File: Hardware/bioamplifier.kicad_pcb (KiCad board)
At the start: 4 copper layers, 70 x 40 mm, 92 parts, among them IC1 MCP1754ST-3302E_DB, J1 Conn_01x07_Socket, J2 Conn_01x26_Pin, J3 Conn_01x07_Socket, U1 ADS1299IPAG, U10 TPD4E1B06DCKR, U11 LM2665M6, U2 TPD4E1B06DCKR, U3 TPD4E1B06DCKR, U4 TPD4E1B06DCKR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

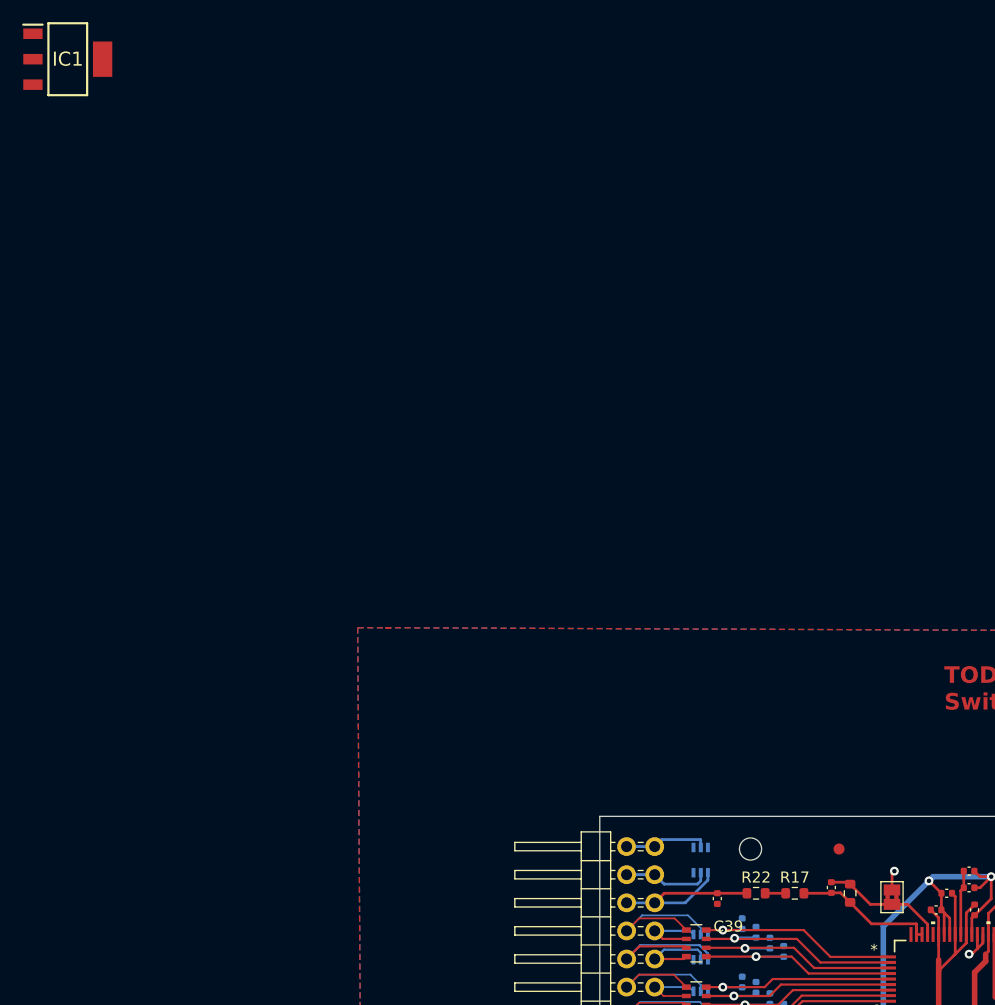
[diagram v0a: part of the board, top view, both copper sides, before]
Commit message: Remove redundant components
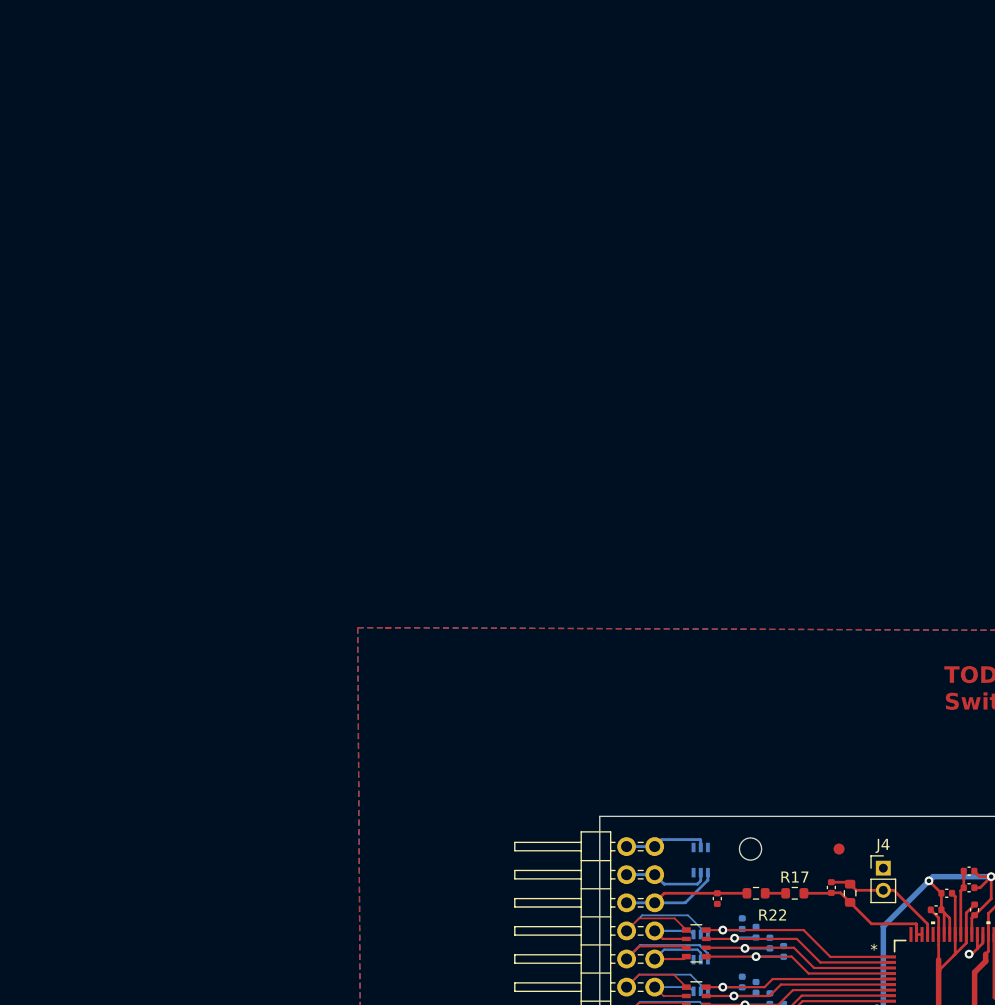
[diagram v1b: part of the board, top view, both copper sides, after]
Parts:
- removed IC1: MCP1754ST-3302E_DB, mcp1754:SOT230P700X180-4N
- removed JP2: Jumper_2_Bridged, Jumper:SolderJumper-2_P1.3mm_Bridged2Bar_Pad1.0x1.5mm
- added J4: Jumper, Connector_PinHeader_2.00mm:PinHeader_1x02_P2.00mm_Vertical, F.Cu at (78.0, 76.7)
- C25, C40: value 0.1u -> 0.1uF
- C45, C46: value 10 u -> 10 uF
- R1: value 1K -> 1 KΩ
- R10, R11, R12, R13, R14, R3, R4, R5, R6, R7, R8, R9: value 50 -> 50 Ω
- R17: value 1M -> 1 MΩ
- R18, R2, R20, R22, RN1, RN2, RN3, RN4: value 4.99 K -> 4.99 KΩ
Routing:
- net GNDA: track 33.5 -> 31.7 mm, vias 8 -> 7

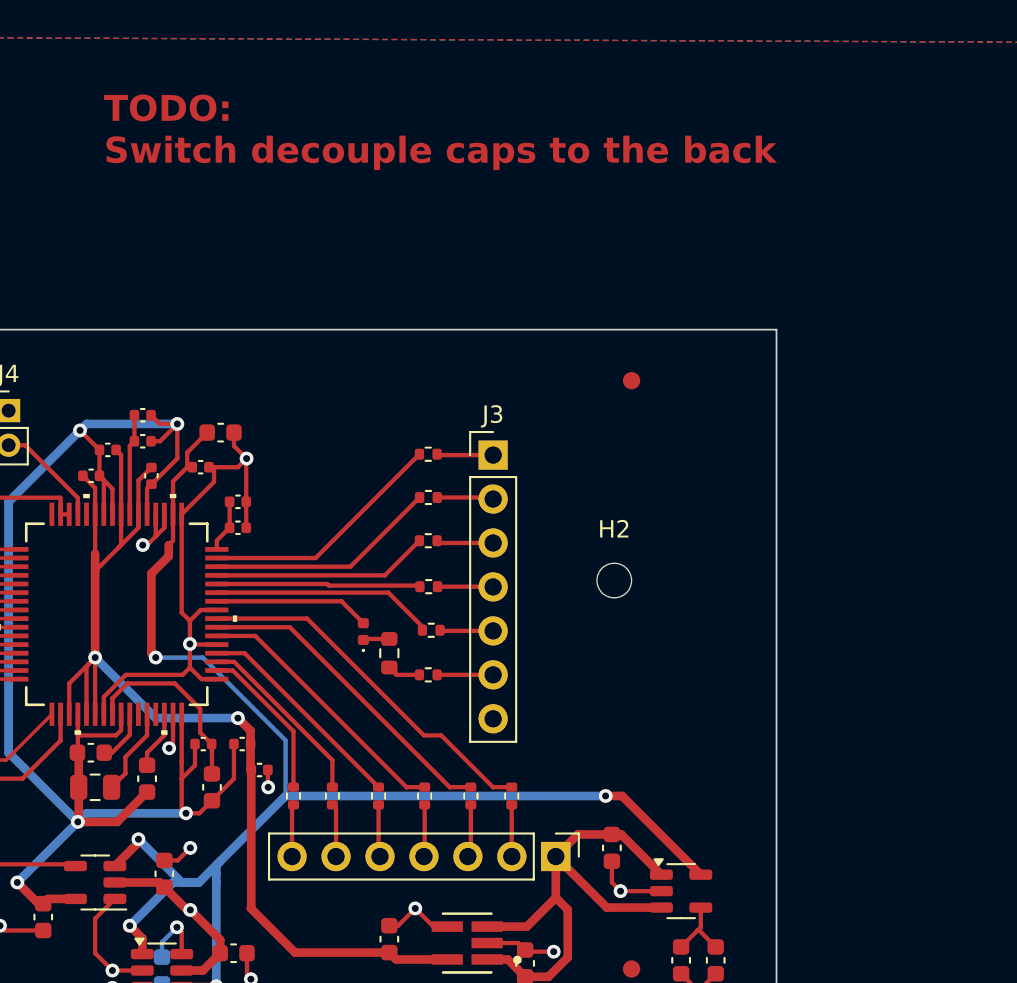
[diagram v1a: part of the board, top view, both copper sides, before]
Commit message: Add Daisychain jumper
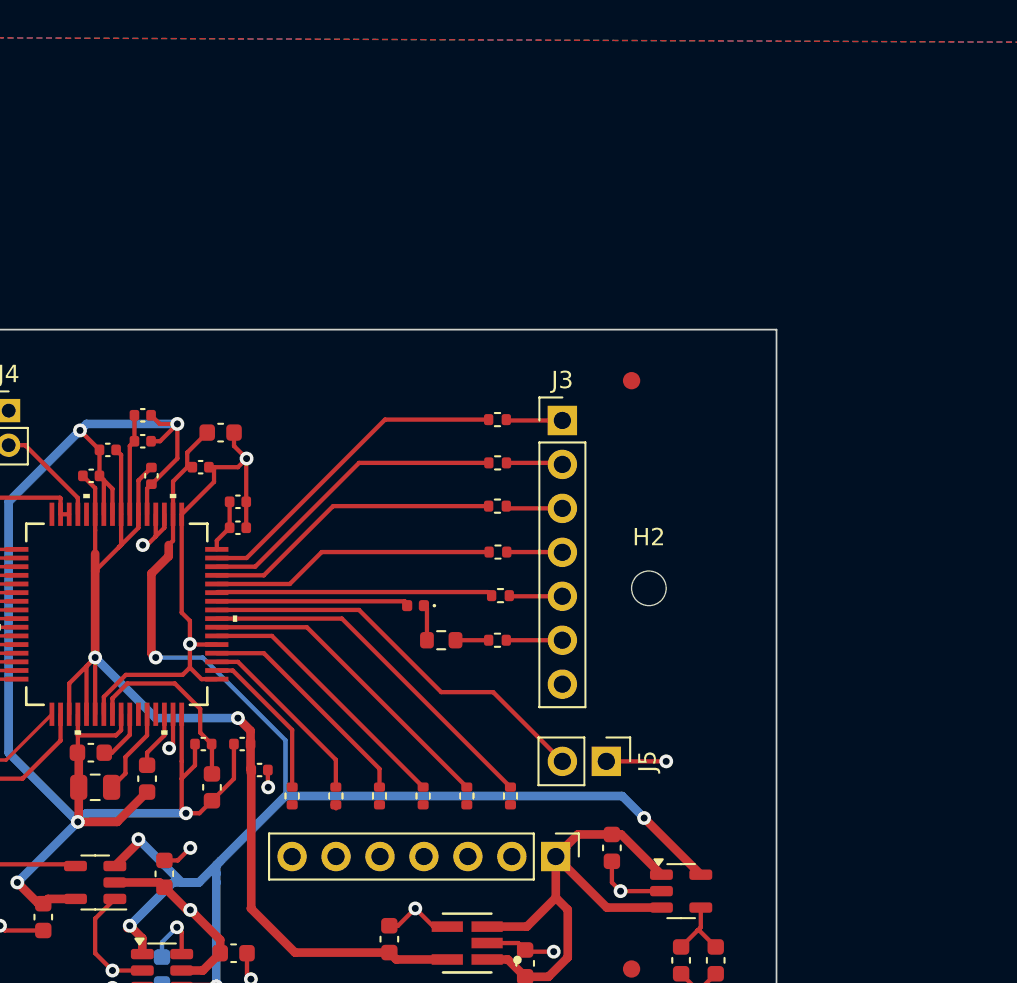
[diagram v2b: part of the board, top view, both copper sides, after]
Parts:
- added J5: Jumper, Connector_PinHeader_2.54mm:PinHeader_1x02_P2.54mm_Vertical, F.Cu at (112.5, 97.0)
- D1: value BLUE LED -> LB QH9G-N1OO-35-1
- RN1, RN2, RN3, RN4: value 4.99 KΩ -> EXB-V8V512JV
- moved J3 4.47 mm to (110.0, 77.3)
- moved R3 4.47 mm to (106.2, 77.2)
- moved R4 4.47 mm to (106.3, 79.8)
- moved R5 4.47 mm to (106.2, 82.2)
- moved R6 4.47 mm to (106.3, 84.9)
- moved R7 4.47 mm to (106.4, 87.4)
- moved R8 4.47 mm to (106.2, 90.0)
- moved D1 3.37 mm to (101.5, 88.0), turned to 180 degrees
- moved R1 3.09 mm to (103.0, 90.0), turned to 0 degrees
- moved H2 2.05 mm to (115.0, 87.0)
- moved R10 0.23 mm to (104.5, 99.0)
- moved R13 0.20 mm to (96.9, 99.0)
- moved R11 0.09 mm to (102.0, 99.0)
- moved R9 0.07 mm to (107.0, 99.0)
- moved R14 0.07 mm to (94.4, 99.0)
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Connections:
- U1 pad 41: GNDD -> /DAISY-IN
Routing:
- net /DAISY-IN: track 0.00 -> 23.6 mm
- net /GPIO4: track 13.4 -> 18.2 mm
- net /GPIO3: track 12.5 -> 17.4 mm
- net /DRDY: track 14.2 -> 19.0 mm
- net /GPIO2: track 11.8 -> 16.5 mm
- net /DOUT: track 12.9 -> 16.0 mm
- net Net-(J1-Pin_2): track 2.99 -> 0.01 mm
- net Net-(J1-Pin_4): track 3.01 -> 0.06 mm
- net Net-(J1-Pin_7): track 3.02 -> 0.11 mm
- net Net-(J1-Pin_5): track 3.02 -> 0.12 mm
- net Net-(J1-Pin_3): track 3.06 -> 0.24 mm
- net Net-(J1-Pin_6): track 3.08 -> 0.30 mm
- net Net-(D1-A): track 9.00 -> 11.0 mm
- net GNDD: track 44.9 -> 46.6 mm, vias 6 -> 7
- net Net-(D1-K): track 1.52 -> 2.22 mm
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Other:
- board text removed: "TODO: Switch decouple caps to the back"

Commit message: Fix unconnected components
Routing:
- net Net-(J1-Pin_3): track 0.24 -> 3.26 mm
- net Net-(J1-Pin_2): track 0.01 -> 3.02 mm
- net Net-(J1-Pin_4): track 0.06 -> 3.07 mm
- net Net-(J1-Pin_5): track 0.12 -> 3.12 mm
- net Net-(J1-Pin_6): track 0.30 -> 3.29 mm
- net Net-(J1-Pin_7): track 0.11 -> 3.11 mm
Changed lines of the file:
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@@
+	)
+	(segment
+		(start 94.38 99.515557)
+		(end 94.385557 99.51)
+		(width 0.25)
+		(layer "F.Cu")
+		(net 67)
+	)
+	(segment
+		(start 94.38 102.5)
+		(end 94.38 99.515557)
+		(width 0.25)
+		(layer "F.Cu")
+		(net 67)
 	)
 	(segment
@@
 	)
 	(segment
+		(start 102 102.5)
+		(end 102 99.555777)
+		(width 0.25)
+		(layer "F.Cu")
+		(net 68)
+	)
+	(segment
+		(start 102 99.555777)
+		(end 101.954223 99.51)
+		(width 0.25)
+		(layer "F.Cu")
+		(net 68)
+	)
+	(segment
+		(start 96.92 102.5)
+		(end 96.92 99.521554)
+		(width 0.25)
+		(layer "F.Cu")
+		(net 69)
+	)
+	(segment
 		(start 96.92 99.72)
 		(end 96.71 99.51)
@@
 		(layer "F.Cu")
 		(net 69)
+	)
+	(segment
+		(start 96.92 99.521554)
+		(end 96.908446 99.51)
+		(width 0.25)
+		(layer "F.Cu")
+		(net 69)
+	)
+	(segment
+		(start 104.54 102.5)
+		(end 104.54 99.572889)
+		(width 0.25)
+		(layer "F.Cu")
+		(net 70)
 	)
 	(segment
@@
 	)
 	(segment
+		(start 104.54 99.572889)
+		(end 104.477111 99.51)
+		(width 0.25)
+		(layer "F.Cu")
+		(net 70)
+	)
+	(segment
+		(start 99.46 102.5)
+		(end 99.46 99.538666)
+		(width 0.25)
+		(layer "F.Cu")
+		(net 71)
+	)
+	(segment
 		(start 99.376666 102.416666)
 		(end 99.46 102.5)
@@
 	)
 	(segment
-		(start 107.074443 102.494443)
+		(start 99.46 99.538666)
+		(end 99.431334 99.51)
+		(width 0.25)
+		(layer "F.Cu")
+		(net 71)
+	)
+	(segment
+		(start 107 99.51)
+		(end 107 102.42)
+		(width 0.25)
+		(layer "F.Cu")
+		(net 72)
+	)
+	(segment
+		(start 107 102.42)
 		(end 107.08 102.5)
 		(width 0.25)

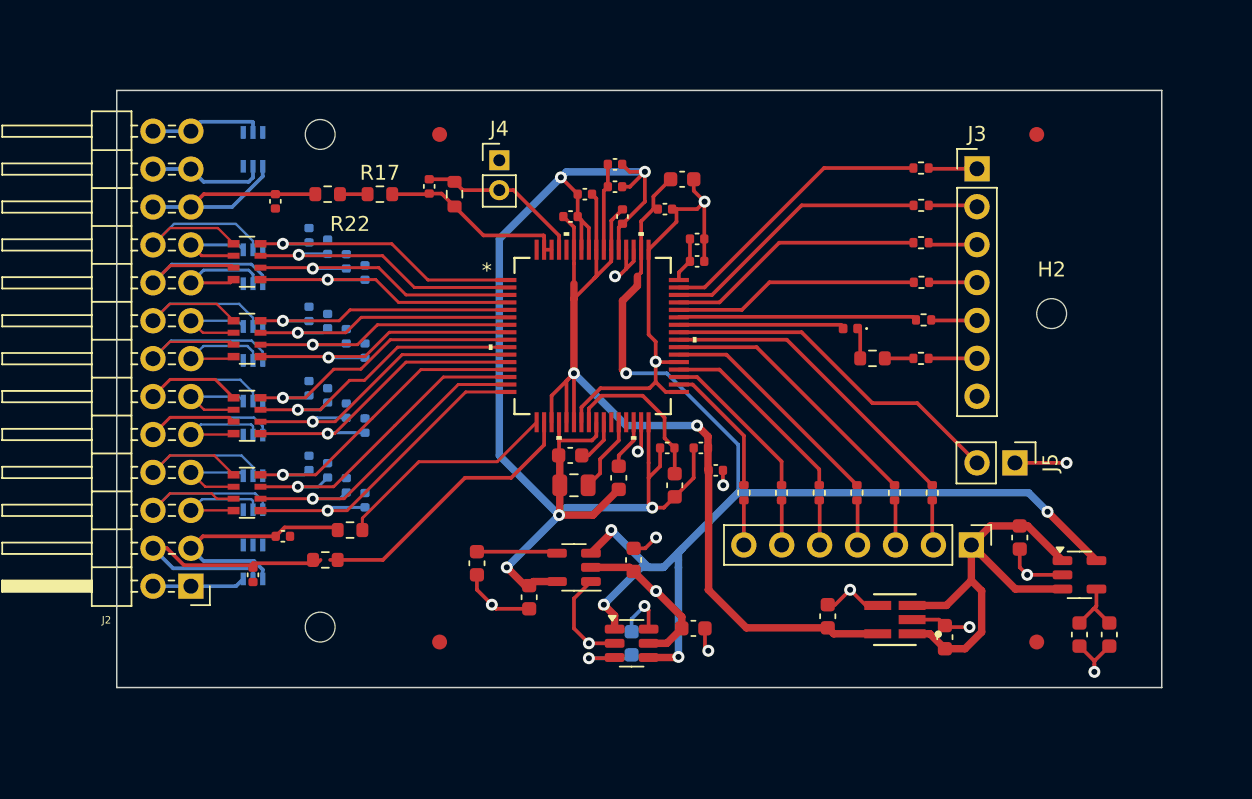
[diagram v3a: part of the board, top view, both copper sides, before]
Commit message: Add poweron Led
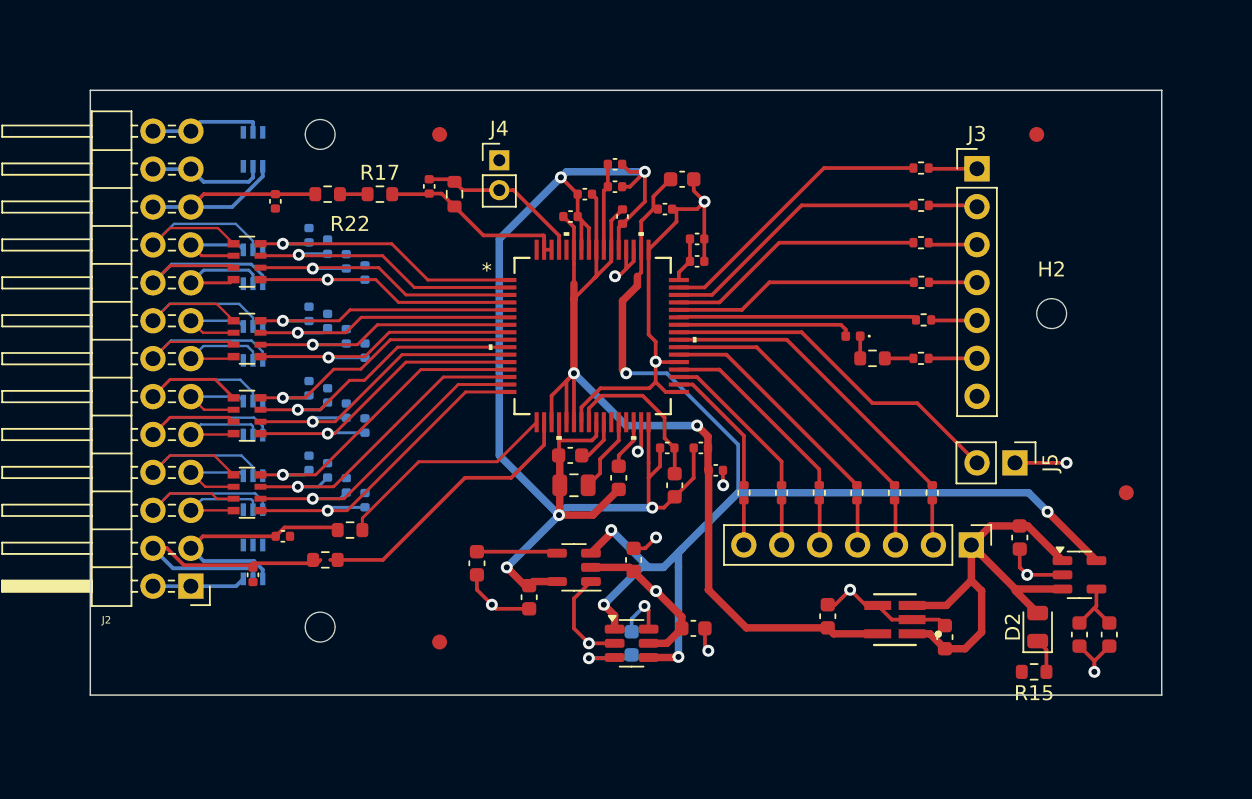
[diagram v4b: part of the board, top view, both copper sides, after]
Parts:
- added D2: HSMH-H170, LED_SMD:LED_0805_2012Metric, F.Cu at (114.1, 108.0)
- added R15: 180 Ω, Resistor_SMD:R_0603_1608Metric, F.Cu at (113.8, 111.0)
- moved FID2 11.7 mm to (120.0, 99.0)
- moved D1 0.54 mm to (101.7, 88.5)
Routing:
- net Net-(D2-K): track 0.00 -> 2.31 mm
- net 3.3V_UNREG: track 31.2 -> 33.5 mm
- net GNDA: track 31.7 -> 32.9 mm, vias 7 -> 6
- net Net-(D1-A): track 11.0 -> 11.8 mm
- net Net-(D1-K): track 2.22 -> 1.49 mm
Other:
- board size 70 x 40 mm -> 71.8 x 40.5 mm
